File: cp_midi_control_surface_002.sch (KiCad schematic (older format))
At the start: 23 parts, among them P1 Power, P2 Analogue, P3 Digital, P4 Communication, P5 PWM, P6 PWM

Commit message: Forgot to update a couple of components
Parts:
- JA4, JA6: footprint Connector_PinHeader_2.54mm:PinHeader_2x03_P2.54mm_Vertical -> Connector_PinHeader_2.54mm:PinHeader_2x05_P2.54mm_Vertical; symbol Connector:Conn_01x06_Male -> Connector:Conn_01x10_Male
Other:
- moved on the sheet: JA8
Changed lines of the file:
@@
 Wire Wire Line
 	8650 5050 8650 5550
-Text Label 6450 4650 0    50   ~ 0
+Text Label 6450 5450 0    50   ~ 0
 A0
 $Comp
@@
 	-1   0    0    -1
 $EndComp
-Text Label 6450 3650 0    50   ~ 0
+Text Label 6450 4050 0    50   ~ 0
 A5
 $Comp
-L Connector:Conn_01x06_Male JA6
+L Connector:Conn_01x10_Male JA6
 U 1 1 5CD77852
-P 6150 3450
-F 0 "JA6" H 6150 3900 50  0000 L CNN
-F 1 "~" H 6177 3335 50  0000 L CNN
-F 2 "Connector_PinHeader_2.54mm:PinHeader_2x03_P2.54mm_Vertical" H 6150 3450 50  0001 C CNN
-F 3 "~" H 6150 3450 50  0001 C CNN
-	1    6150 3450
-	1    0    0    -1
-$EndComp
-Wire Wire Line
-	6600 3550 6350 3550
-Wire Wire Line
-	6600 3450 6350 3450
-Wire Wire Line
-	6600 3350 6350 3350
-Wire Wire Line
-	6600 3250 6350 3250
+P 6150 4050
+F 0 "JA6" H 6150 4700 50  0000 L CNN
+F 1 "~" H 6177 3935 50  0000 L CNN
+F 2 "Connector_PinHeader_2.54mm:PinHeader_2x05_P2.54mm_Vertical" H 6150 4050 50  0001 C CNN
+F 3 "~" H 6150 4050 50  0001 C CNN
+	1    6150 4050
+	1    0    0    -1
+$EndComp
+Wire Wire Line
+	6600 3950 6350 3950
+Wire Wire Line
+	6600 3850 6350 3850
+Wire Wire Line
+	6600 3750 6350 3750
+Wire Wire Line
+	6600 3650 6350 3650
 Text Label 6450 2650 0    50   ~ 0
 A3
 $Comp
-L Connector:Conn_01x06_Male JA4
+L Connector:Conn_01x10_Male JA4
 U 1 1 5CD8ED92
-P 6150 2450
-F 0 "JA4" H 6150 2900 50  0000 L CNN
-F 1 "~" H 6177 2335 50  0000 L CNN
-F 2 "Connector_PinHeader_2.54mm:PinHeader_2x03_P2.54mm_Vertical" H 6150 2450 50  0001 C CNN
-F 3 "~" H 6150 2450 50  0001 C CNN
-	1    6150 2450
-	1    0    0    -1
-$EndComp
-Wire Wire Line
-	6600 2550 6350 2550
-Wire Wire Line
-	6600 2450 6350 2450
+P 6150 2650
+F 0 "JA4" H 6150 3300 50  0000 L CNN
+F 1 "~" H 6177 2535 50  0000 L CNN
+F 2 "Connector_PinHeader_2.54mm:PinHeader_2x05_P2.54mm_Vertical" H 6150 2650 50  0001 C CNN
+F 3 "~" H 6150 2650 50  0001 C CNN
+	1    6150 2650
+	1    0    0    -1
+$EndComp
 Wire Wire Line
 	6600 2350 6350 2350
@@
 L Connector:Conn_01x06_Male JA8
 U 1 1 5CDA24B3
-P 6150 4450
-F 0 "JA8" H 6150 4900 50  0000 L CNN
-F 1 "~" H 6177 4335 50  0000 L CNN
-F 2 "Connector_PinHeader_2.54mm:PinHeader_2x03_P2.54mm_Vertical" H 6150 4450 50  0001 C CNN
-F 3 "~" H 6150 4450 50  0001 C CNN
-	1    6150 4450
-	1    0    0    -1
-$EndComp
-Wire Wire Line
-	6600 4550 6350 4550
-Wire Wire Line
-	6600 4450 6350 4450
-Wire Wire Line
-	6600 4350 6350 4350
-Wire Wire Line
-	6600 4250 6350 4250
-Wire Wire Line
-	6450 4650 6350 4650
-Wire Wire Line
-	6450 3650 6350 3650
+P 6150 5250
+F 0 "JA8" H 6150 5700 50  0000 L CNN
+F 1 "~" H 6177 5135 50  0000 L CNN
+F 2 "Connector_PinHeader_2.54mm:PinHeader_2x03_P2.54mm_Vertical" H 6150 5250 50  0001 C CNN
+F 3 "~" H 6150 5250 50  0001 C CNN
+	1    6150 5250
+	1    0    0    -1
+$EndComp
+Wire Wire Line
+	6600 5350 6350 5350
+Wire Wire Line
+	6600 5250 6350 5250
+Wire Wire Line
+	6600 5150 6350 5150
+Wire Wire Line
+	6600 5050 6350 5050
+Wire Wire Line
+	6450 5450 6350 5450
+Wire Wire Line
+	6450 4050 6350 4050
 Wire Wire Line
 	6450 2650 6350 2650
@@
 Wire Wire Line
 	7150 1750 7150 1000
-Connection ~ 7150 1750
 Wire Wire Line
 	7150 1750 6350 1750
-Connection ~ 7150 3750
 Wire Wire Line
 	7150 2750 6350 2750
 Wire Wire Line
-	7150 3750 7150 4750
-Wire Wire Line
-	7150 3750 6350 3750
-Wire Wire Line
-	7150 4750 6350 4750
-Wire Wire Line
-	7150 1750 7150 2750
-Connection ~ 7150 2750
-Wire Wire Line
-	7150 2750 7150 3750
+	7150 4150 6350 4150
 Text GLabel 6600 1250 2    50   Input ~ 0
 S0
@@
 Text GLabel 6600 1450 2    50   Input ~ 0
 S3
-Text GLabel 6600 3250 2    50   Input ~ 0
+Text GLabel 6600 3650 2    50   Input ~ 0
 S0
-Text GLabel 6600 3350 2    50   Input ~ 0
+Text GLabel 6600 3750 2    50   Input ~ 0
 S1
-Text GLabel 6600 3550 2    50   Input ~ 0
+Text GLabel 6600 3950 2    50   Input ~ 0
 S2
-Text GLabel 6600 3450 2    50   Input ~ 0
+Text GLabel 6600 3850 2    50   Input ~ 0
 S3
-Text GLabel 6600 4250 2    50   Input ~ 0
+Text GLabel 6600 5050 2    50   Input ~ 0
 S0
-Text GLabel 6600 4350 2    50   Input ~ 0
+Text GLabel 6600 5150 2    50   Input ~ 0
 S1
-Text GLabel 6600 4550 2    50   Input ~ 0
+Text GLabel 6600 5350 2    50   Input ~ 0
 S2
-Text GLabel 6600 4450 2    50   Input ~ 0
+Text GLabel 6600 5250 2    50   Input ~ 0
 S3
 Wire Wire Line
@@
 Wire Wire Line
 	1150 6700 1150 6850
+Wire Wire Line
+	6600 2450 6350 2450
+Wire Wire Line
+	6600 2550 6350 2550
+Connection ~ 7150 2750
+Connection ~ 7150 4150
+Wire Wire Line
+	6350 5550 7150 5550
+Wire Wire Line
+	7150 4150 7150 5550
+Wire Wire Line
+	7150 2750 7150 4150
+Wire Wire Line
+	7150 1750 7150 2750
+Connection ~ 7150 1750
 $EndSCHEMATC

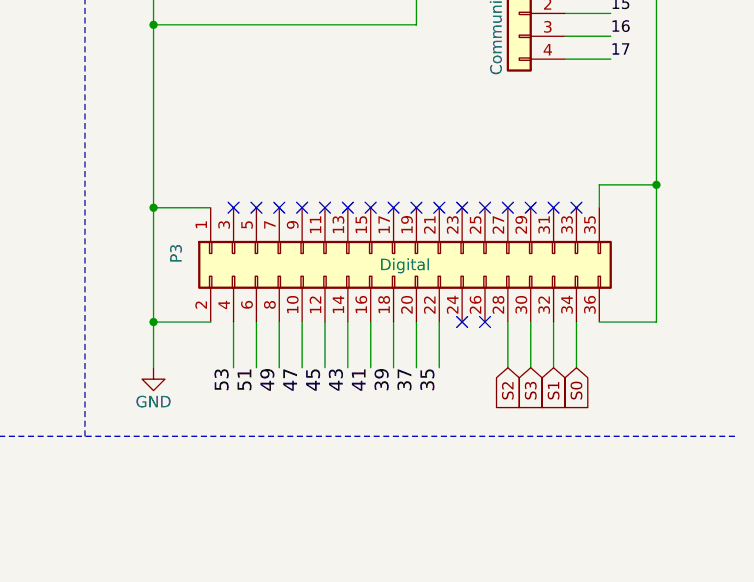
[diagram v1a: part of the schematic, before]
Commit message: Housekeeping
Cleaned up the schematic for the subsidiary boards

Switched 5v and Com connections to make routing easier.
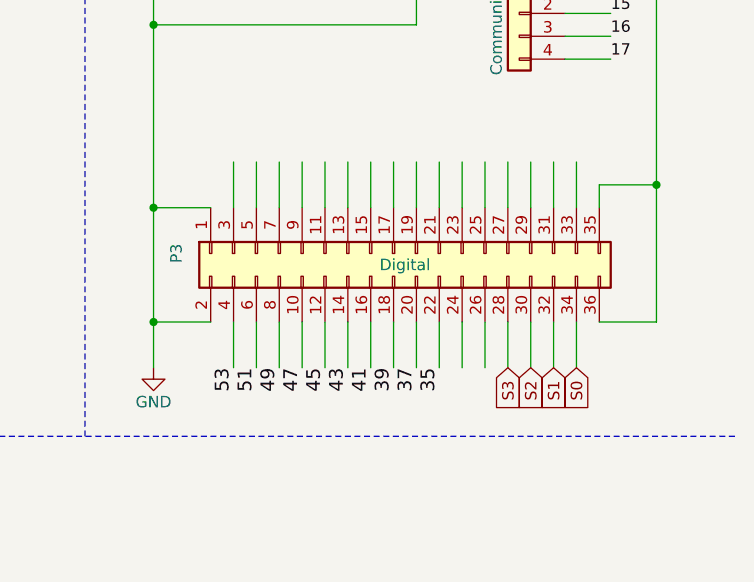
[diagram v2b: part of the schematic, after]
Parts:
- P2: footprint Connector_PinHeader_2.54mm:PinHeader_1x08_P2.54mm_Vertical -> Connector_PinHeader_2.54mm:PinHeader_1x06_P2.54mm_Vertical
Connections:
- wire segments 150 -> 168
- no-connect marks 79 -> 61
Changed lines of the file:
@@
 F 0 "P2" H 9250 3650 50  0000 C CNN
 F 1 "Analogue" V 9350 3250 50  0000 C CNN
-F 2 "Connector_PinHeader_2.54mm:PinHeader_1x08_P2.54mm_Vertical" H 9250 3250 50  0001 C CNN
+F 2 "Connector_PinHeader_2.54mm:PinHeader_1x06_P2.54mm_Vertical" H 9250 3250 50  0001 C CNN
 F 3 "" H 9250 3250 50  0000 C CNN
 	1    9250 3250
@@
 Text GLabel 10400 5750 3    50   Input ~ 0
 S1
+Text GLabel 10300 5750 3    50   Input ~ 0
+S2
 Text GLabel 10200 5750 3    50   Input ~ 0
-S2
-Text GLabel 10300 5750 3    50   Input ~ 0
 S3
 NoConn ~ 9050 3550
@@
 Text Notes 6650 600  0    50   ~ 0
 Connections on main board
-NoConn ~ 10000 5550
-NoConn ~ 10100 5550
 Wire Wire Line
 	8900 5550 8650 5550
@@
 	10850 4950 10850 5550
 Connection ~ 10850 4950
-NoConn ~ 9000 5050
-NoConn ~ 9100 5050
-NoConn ~ 9200 5050
-NoConn ~ 9300 5050
-NoConn ~ 9400 5050
-NoConn ~ 9500 5050
-NoConn ~ 9600 5050
-NoConn ~ 9700 5050
-NoConn ~ 9800 5050
-NoConn ~ 9900 5050
-NoConn ~ 10000 5050
-NoConn ~ 10100 5050
-NoConn ~ 10200 5050
-NoConn ~ 10300 5050
-NoConn ~ 10400 5050
-NoConn ~ 10500 5050
 $Comp
 L power:GND #PWR?
@@
 	7150 1750 7150 2750
 Connection ~ 7150 1750
+Wire Wire Line
+	10000 5550 10000 5750
+Wire Wire Line
+	10100 5550 10100 5750
+Wire Wire Line
+	10300 4850 10300 5050
+Wire Wire Line
+	10200 4850 10200 5050
+Wire Wire Line
+	9900 4850 9900 5050
+Wire Wire Line
+	9800 4850 9800 5050
+Wire Wire Line
+	9700 4850 9700 5050
+Wire Wire Line
+	9600 4850 9600 5050
+Wire Wire Line
+	9500 4850 9500 5050
+Wire Wire Line
+	9400 4850 9400 5050
+Wire Wire Line
+	9300 4850 9300 5050
+Wire Wire Line
+	9200 4850 9200 5050
+Wire Wire Line
+	9100 4850 9100 5050
+Wire Wire Line
+	9000 4850 9000 5050
+Wire Wire Line
+	10400 5050 10400 4850
+Wire Wire Line
+	10500 5050 10500 4850
+Wire Wire Line
+	10000 4850 10000 5050
+Wire Wire Line
+	10100 4850 10100 5050
 $EndSCHEMATC

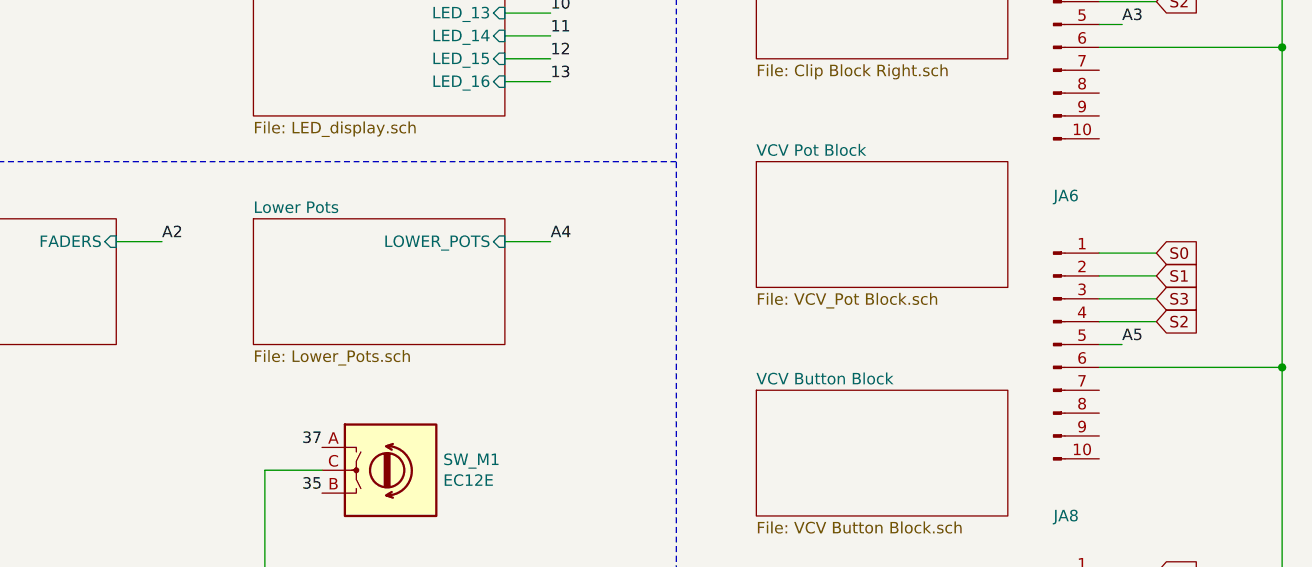
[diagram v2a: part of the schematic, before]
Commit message: Reordered COM contacts and added initial trace positions
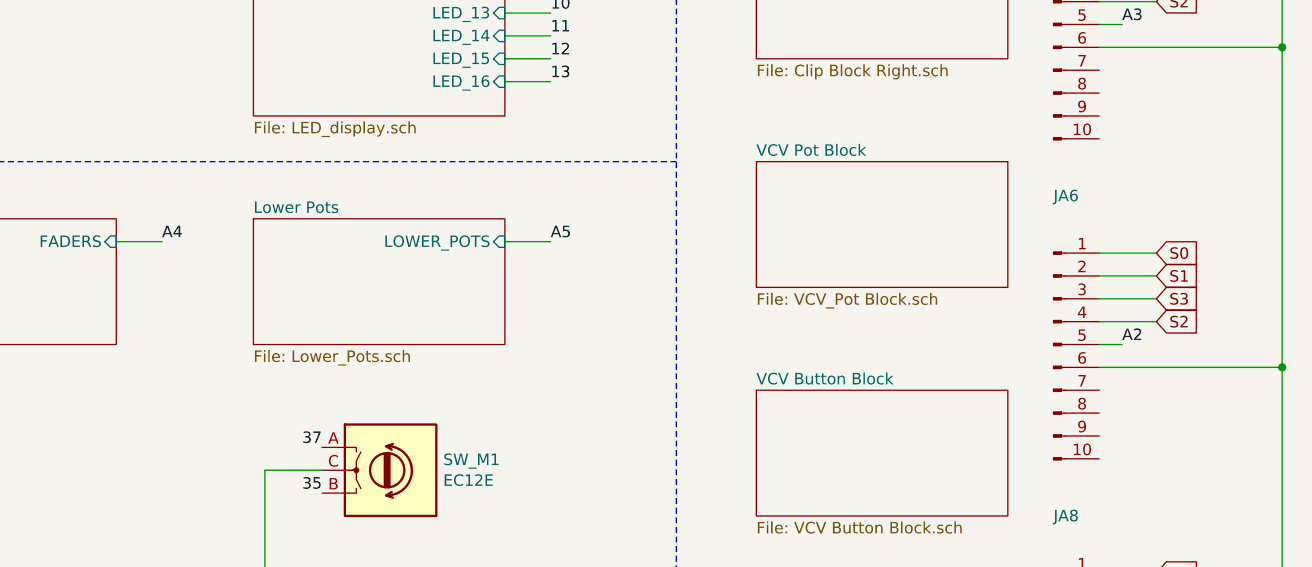
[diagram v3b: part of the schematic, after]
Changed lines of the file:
@@
 $EndSheet
 Text Label 3950 3600 0    50   ~ 0
-A4
+A5
 Wire Wire Line
 	3750 3600 3950 3600
@@
 $EndComp
 Text Label 6450 4050 0    50   ~ 0
-A5
+A2
 $Comp
 L Connector:Conn_01x10_Male JA6
@@
 	10500 5750 10500 5550
 Text Label 2250 3600 0    50   ~ 0
-A2
+A4
 Wire Wire Line
 	2050 3600 2250 3600

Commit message: Reinstated extra two pins. Probably coming out again later.
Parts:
- P2: footprint Connector_PinHeader_2.54mm:PinHeader_1x06_P2.54mm_Vertical -> Connector_PinHeader_2.54mm:PinHeader_1x08_P2.54mm_Vertical
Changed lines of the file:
@@
 F 0 "P2" H 9250 3650 50  0000 C CNN
 F 1 "Analogue" V 9350 3250 50  0000 C CNN
-F 2 "Connector_PinHeader_2.54mm:PinHeader_1x06_P2.54mm_Vertical" H 9250 3250 50  0001 C CNN
+F 2 "Connector_PinHeader_2.54mm:PinHeader_1x08_P2.54mm_Vertical" H 9250 3250 50  0001 C CNN
 F 3 "" H 9250 3250 50  0000 C CNN
 	1    9250 3250

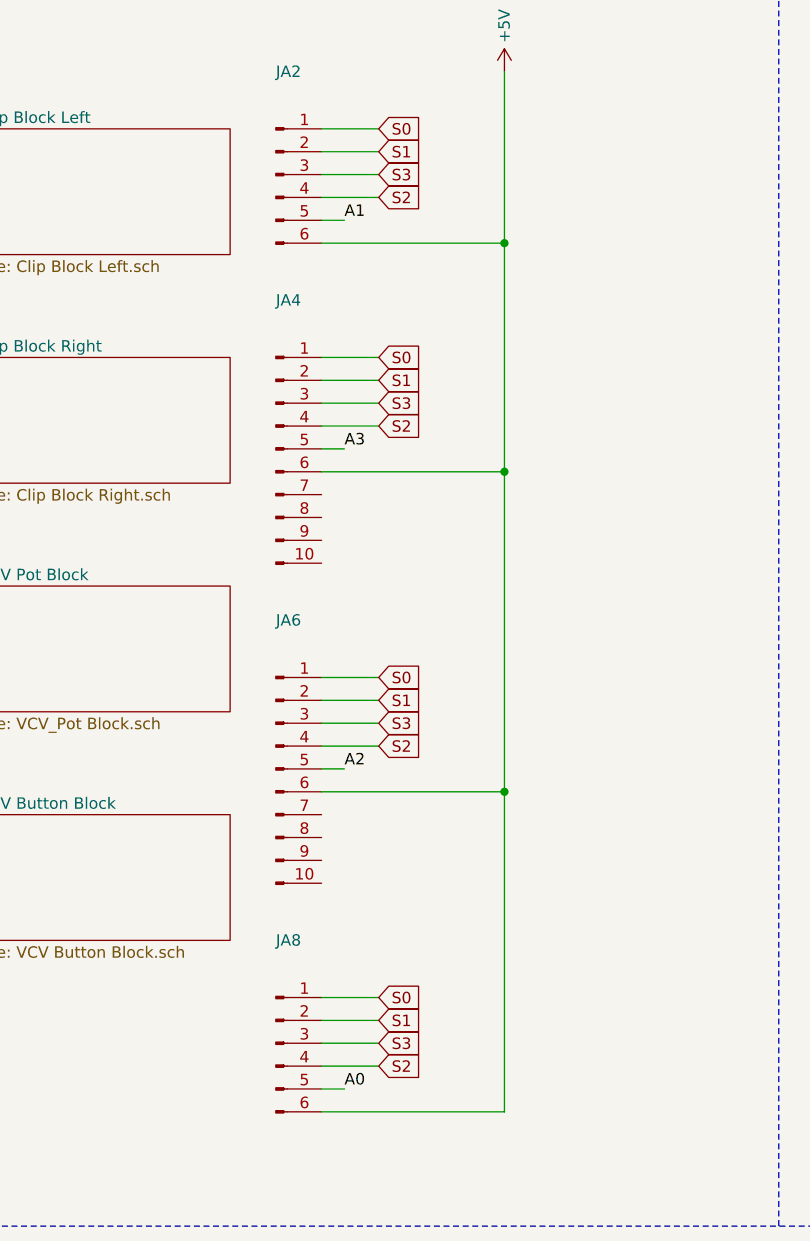
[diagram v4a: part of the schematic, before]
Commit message: Fixed S0-S3 Rail, added LEDS
Was an error on the schematic, easily fixed without changing the traces, glad I left it before deleting them all.

LEDs and relate resistors are in.
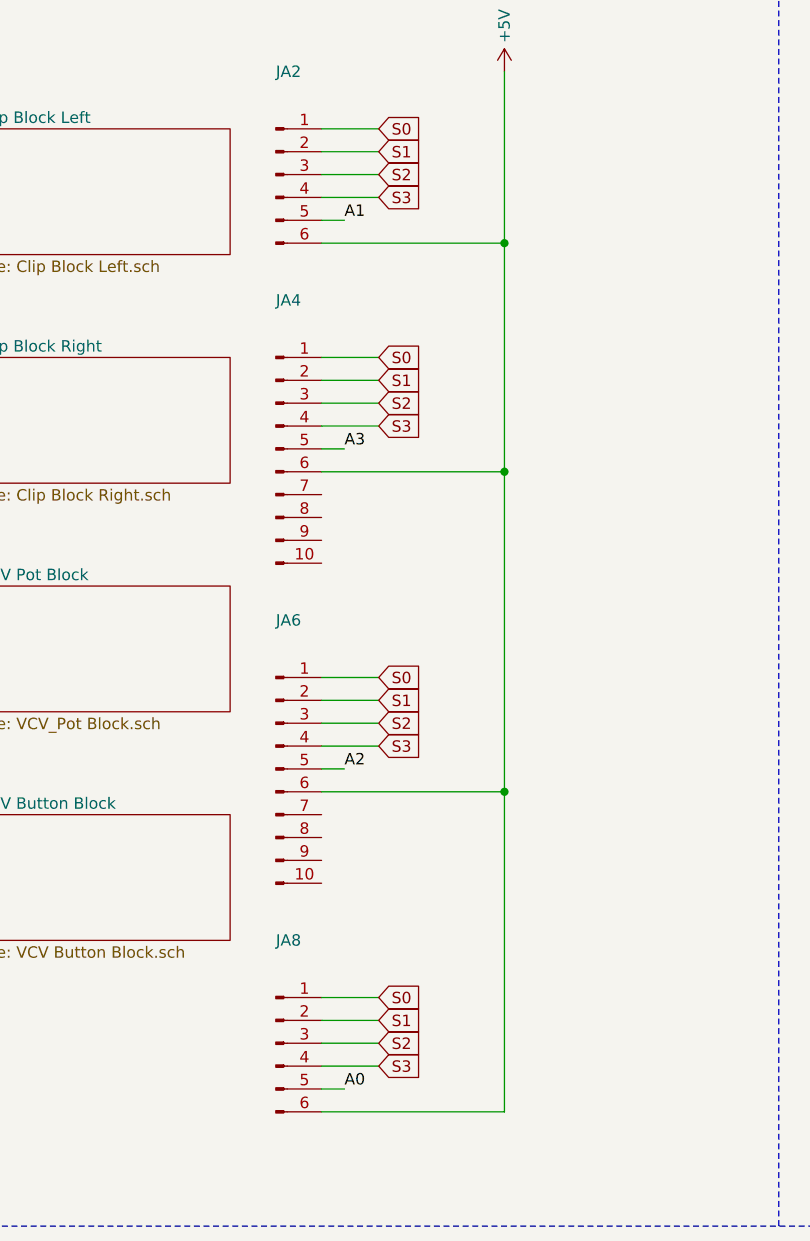
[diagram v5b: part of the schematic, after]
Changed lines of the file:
@@
 Text GLabel 6600 2350 2    50   Input ~ 0
 S1
+Text GLabel 6600 2450 2    50   Input ~ 0
+S2
 Text GLabel 6600 2550 2    50   Input ~ 0
-S2
-Text GLabel 6600 2450 2    50   Input ~ 0
 S3
 Wire Wire Line
@@
 Text GLabel 6600 1350 2    50   Input ~ 0
 S1
+Text GLabel 6600 1450 2    50   Input ~ 0
+S2
 Text GLabel 6600 1550 2    50   Input ~ 0
-S2
-Text GLabel 6600 1450 2    50   Input ~ 0
 S3
 Text GLabel 6600 3650 2    50   Input ~ 0
@@
 Text GLabel 6600 3750 2    50   Input ~ 0
 S1
+Text GLabel 6600 3850 2    50   Input ~ 0
+S2
 Text GLabel 6600 3950 2    50   Input ~ 0
-S2
-Text GLabel 6600 3850 2    50   Input ~ 0
 S3
 Text GLabel 6600 5050 2    50   Input ~ 0
@@
 Text GLabel 6600 5150 2    50   Input ~ 0
 S1
+Text GLabel 6600 5250 2    50   Input ~ 0
+S2
 Text GLabel 6600 5350 2    50   Input ~ 0
-S2
-Text GLabel 6600 5250 2    50   Input ~ 0
 S3
 Wire Wire Line

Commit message: Added external connections / removed unused
+18 Buttons
+ Different connections for 7 spare multiplexer slots
- Unused Arduino pins
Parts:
- JA4: footprint Connector_PinHeader_2.54mm:PinHeader_2x05_P2.54mm_Vertical -> Connector_PinHeader_2.54mm:PinHeader_2x18_P2.54mm_Vertical; symbol Connector:Conn_01x10_Male -> Connector_Generic:Conn_02x18_Odd_Even
- P1: footprint Connector_PinHeader_2.54mm:PinHeader_1x08_P2.54mm_Vertical -> Connector_PinHeader_2.54mm:PinHeader_1x02_P2.54mm_Vertical; symbol Connector_Generic:Conn_01x08 -> Connector_Generic:Conn_01x02
- P2, P5: footprint Connector_PinHeader_2.54mm:PinHeader_1x08_P2.54mm_Vertical -> Connector_PinHeader_2.54mm:PinHeader_1x06_P2.54mm_Vertical; symbol Connector_Generic:Conn_01x08 -> Connector_Generic:Conn_01x06
- P6: footprint Connector_PinHeader_2.54mm:PinHeader_1x10_P2.54mm_Vertical -> Connector_PinHeader_2.54mm:PinHeader_1x07_P2.54mm_Vertical; symbol Connector_Generic:Conn_01x10 -> Connector_Generic:Conn_01x07
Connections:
- net labels added: 22, 24, 26, 28, 30, 31, 32, 33, 34, 36, 38, 40, 42, 44, 46, 48, 50, 52
- wire segments 168 -> 167
- no-connect marks 61 -> 48
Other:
- note removed: "1"
- moved on the sheet: JA2, JA6, JA8

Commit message: Nearly there. Switch placed
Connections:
- net +5V: now also JA4.12 (Pin_12)
- net S0: now also JA4.1 (Pin_1)
- net S1: now also JA4.2 (Pin_2)
- net S2: now also JA4.3 (Pin_3)
- net S3: now also JA4.4 (Pin_4)
- net U5_14: now reaches JA4.11 (Pin_11)
- net U5_13: now reaches JA4.13 (Pin_13)
- net U5_12: now reaches JA4.14 (Pin_14)
- net U5_11: now reaches JA4.15 (Pin_15)
- net U5_10: now reaches JA4.16 (Pin_16)
- net U5_9: now reaches JA4.17 (Pin_17)
- net U5_8: now reaches JA4.18 (Pin_18)
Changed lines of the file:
@@
 	2700 4600 2950 4600
 $Sheet
-S 950  3500 1100 550
+S 950  3500 1100 950
 U 5C542024
 F0 "faders" 50
 F1 "faders.sch" 0
 F2 "FADERS" I R 2050 3600 50
+F3 "U5_8" I R 2050 3750 50
+F4 "U5_9" I R 2050 3850 50
+F5 "U5_10" I R 2050 3950 50
+F6 "U5_11" I R 2050 4050 50
+F7 "U5_12" I R 2050 4150 50
+F8 "U5_13" I R 2050 4250 50
+F9 "U5_14" I R 2050 4350 50
 $EndSheet
 Text Label 8850 2950 2    50   ~ 0
@@
 F1 "VCV Button Block.sch" 0
 $EndSheet
-Text Label 3950 3600 0    50   ~ 0
+Text Label 2250 3600 0    50   ~ 0
 A5
 Wire Wire Line
@@
 Wire Wire Line
 	10500 5750 10500 5550
-Text Label 2250 3600 0    50   ~ 0
+Text Label 3950 3600 0    50   ~ 0
 A4
 Wire Wire Line
@@
 	7200 2050 8000 2050
 Connection ~ 8000 2050
-Wire Wire Line
-	8000 2050 8000 4500
 Text Label 7200 3550 0    50   ~ 0
 26
@@
 Text Label 7200 3250 0    50   ~ 0
 34
+Wire Wire Line
+	7200 2350 8000 2350
+Wire Wire Line
+	8000 2050 8000 2350
+Connection ~ 8000 2350
+Wire Wire Line
+	8000 2350 8000 4500
+Text Label 6700 2350 2    50   ~ 0
+U5_14
+Text Label 6700 2450 2    50   ~ 0
+U5_13
+Text Label 7200 2450 0    50   ~ 0
+U5_12
+Text Label 6700 2550 2    50   ~ 0
+U5_11
+Text Label 7200 2550 0    50   ~ 0
+U5_10
+Text Label 6700 2650 2    50   ~ 0
+U5_9
+Text Label 7200 2650 0    50   ~ 0
+U5_8
+Wire Wire Line
+	7200 1850 7350 1850
+Wire Wire Line
+	7200 1950 7350 1950
+Wire Wire Line
+	6550 1850 6700 1850
+Wire Wire Line
+	6550 1950 6700 1950
+Text Label 2250 4350 0    50   ~ 0
+U5_14
+Text Label 2250 4250 0    50   ~ 0
+U5_13
+Text Label 2250 4050 0    50   ~ 0
+U5_11
+Text Label 2250 3850 0    50   ~ 0
+U5_9
+Text Label 2250 4150 0    50   ~ 0
+U5_12
+Text Label 2250 3950 0    50   ~ 0
+U5_10
+Text Label 2250 3750 0    50   ~ 0
+U5_8
+Wire Wire Line
+	2050 3750 2250 3750
+Wire Wire Line
+	2050 3850 2250 3850
+Wire Wire Line
+	2050 3950 2250 3950
+Wire Wire Line
+	2050 4050 2250 4050
+Wire Wire Line
+	2050 4150 2250 4150
+Wire Wire Line
+	2050 4250 2250 4250
+Wire Wire Line
+	2050 4350 2250 4350
 $EndSCHEMATC
